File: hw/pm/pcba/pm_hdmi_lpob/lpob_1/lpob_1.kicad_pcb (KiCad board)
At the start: 2 copper layers, 43.4 x 36 mm, 3 parts, among them J1 HDMI_A_1.4, J2 HDMI_A_1.4, J3 Conn_01x08_Pin

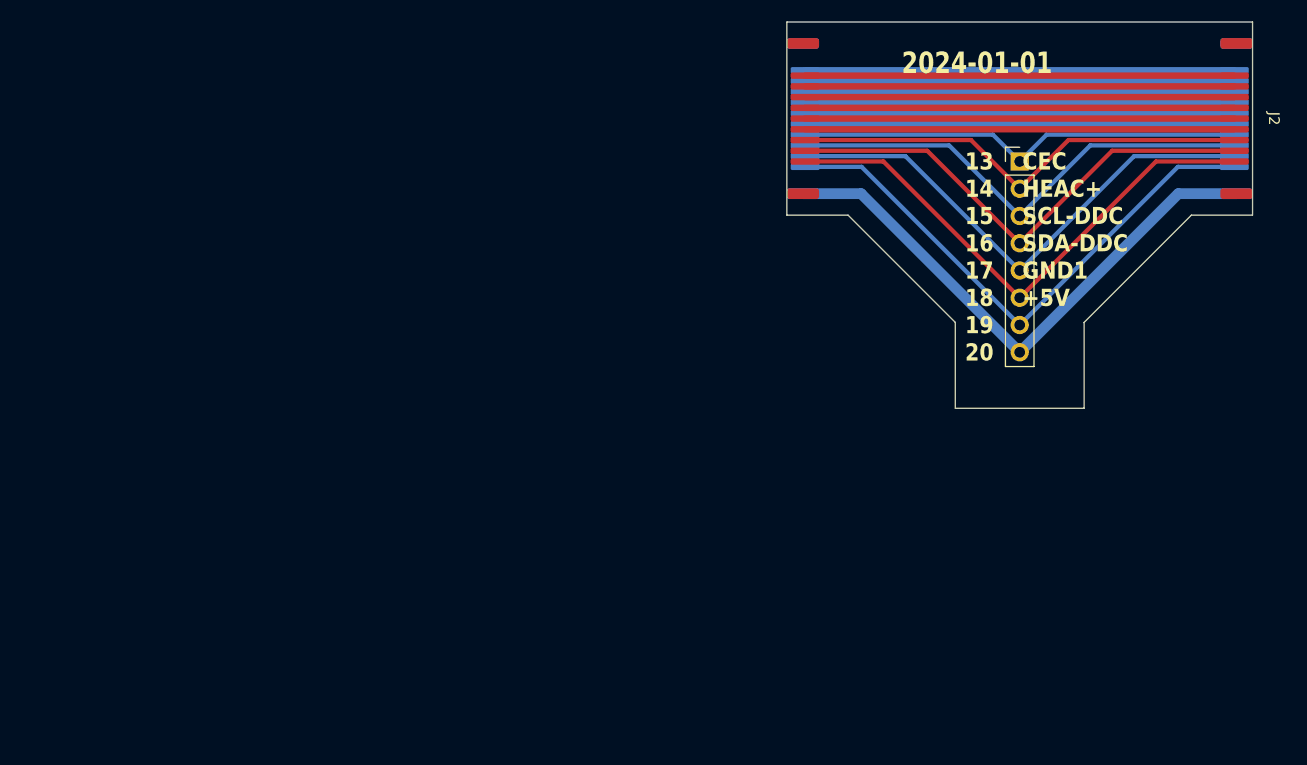
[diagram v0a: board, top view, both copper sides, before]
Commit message: 添加(pm/pcba): 生产 PCB JLC pm_hdmi_lpob v0.1 (2024-01-03)
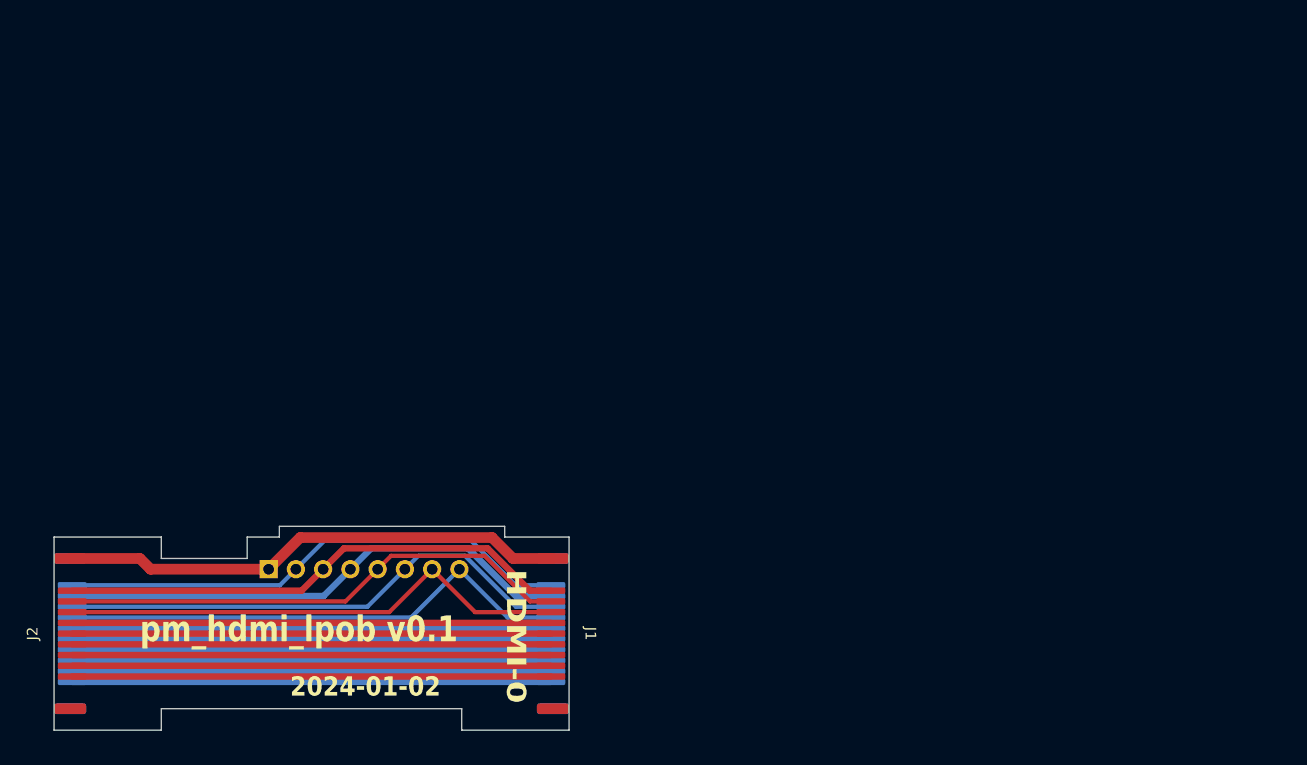
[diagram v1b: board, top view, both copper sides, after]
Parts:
- J1: footprint hdmi_a:hdmi_a_1 -> hdmi_a:hdmi_a_0
- J2: footprint hdmi_a:hdmi_a_2 -> hdmi_a:hdmi_a_1
- J3: moved to B.Cu
- moved J2 121.6 mm to (60.0, 123.0), turned to 90 degrees
- moved J3 79.6 mm to (80.0, 117.0), turned to -90 degrees
- moved J1 52.1 mm to (108.0, 123.0), turned to -90 degrees
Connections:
- J3 pad 1: /P13 -> GND
- J3 pad 2: /P14 -> /P19
- J3 pad 3: /P15 -> /P18
- J3 pad 4: /P16 -> /P17
- J3 pad 5: /P17 -> /P16
- J3 pad 6: /P18 -> /P15
- J3 pad 7: /P19 -> /P14
- J3 pad 8: GND -> /P13
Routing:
- net /P13: track 42.1 -> 48.3 mm
- net GND: track 52.6 -> 47.4 mm
- net Net-(J1-D2S): track 40.0 -> 44.6 mm
- net Net-(J1-D2-): track 40.0 -> 44.6 mm
- net Net-(J1-D2+): track 40.0 -> 44.6 mm
- net Net-(J1-D1S): track 40.0 -> 44.6 mm
- net Net-(J1-D1-): track 40.0 -> 44.6 mm
- net Net-(J1-D1+): track 40.0 -> 44.6 mm
- net Net-(J1-D0S): track 40.0 -> 44.6 mm
- net Net-(J1-D0-): track 40.0 -> 44.6 mm
- net Net-(J1-D0+): track 40.0 -> 44.6 mm
- net Net-(J1-CKS): track 40.0 -> 44.6 mm
- net Net-(J1-CK-): track 40.0 -> 44.6 mm
- net Net-(J1-CK+): track 40.0 -> 44.6 mm
- net /P19: track 52.2 -> 48.0 mm
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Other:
- board size 43.4 x 36 mm -> 48 x 19 mm
- board text added: "19 HEAC-"
- board text added: "20 SH"
- board text added: "2024-01-02"
- board text added: "HDMI-0"
- board text added: "HDMI-1"
- board text removed: "19"
- board text removed: "20"
- board text removed: "2024-01-01"
